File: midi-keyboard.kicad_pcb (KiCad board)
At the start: 2 copper layers, 87 parts, among them J1 ST7735R, SW1 SW_Push_45deg, SW10 SW_Push_45deg, SW11 SW_Push_45deg, SW12 SW_Push_45deg, SW13 SW_Push_45deg, SW14 SW_Push_45deg, SW15 SW_Push_45deg, SW16 SW_Push_45deg, SW17 SW_Push_45deg, SW18 SW_Push_45deg, SW19 SW_Push_45deg, SW2 SW_Push_45deg, SW20 SW_Push_45deg, SW21 SW_Push_45deg, SW22 SW_Push_45deg, SW23 SW_Push_45deg, SW24 SW_Push_45deg, SW25 SW_Push_45deg, SW26 SW_Push_45deg, SW27 SW_Push_45deg, SW28 SW_Push_45deg, SW29 SW_Push_45deg, SW3 SW_Push_45deg, SW30 SW_Push_45deg, SW31 SW_Push_45deg, SW32 SW_Push_45deg, SW33 SW_Push_45deg, SW34 SW_Push_45deg, SW35 SW_Push_45deg, SW36 SW_Push_45deg, SW37 SW_Push_45deg, SW38 SW_Push_45deg, SW39 SW_Push_45deg, SW4 SW_Push_45deg, SW40 SW_Push_45deg, SW42 RotaryEncoder_Switch_MP, SW43 RotaryEncoder_Switch_MP, SW44 SW_Push_45deg, SW5 SW_Push_45deg, SW6 SW_Push_45deg, SW7 SW_Push_45deg, SW8 SW_Push_45deg, SW9 SW_Push_45deg

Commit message: finished pcb tracing
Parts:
- removed D14, D21, D27, D28, D34, D35, D41, D42, D7: 1N4148, Diode_THT:D_DO-35_SOD27_P7.62mm_Horizontal
- removed SW34, SW35, SW36, SW37, SW38, SW39, SW40: SW_Push_45deg, Button_Switch_Keyboard:SW_Cherry_MX_1.00u_PCB
- removed SW42, SW43: RotaryEncoder_Switch_MP, Rotary_Encoder:RotaryEncoder_Alps_EC11E-Switch_Vertical_H20mm_MountingHoles
- J1: value ST7735R -> Conn_01x04; footprint Connector_PinHeader_2.54mm:PinHeader_1x08_P2.54mm_Vertical -> Connector_PinSocket_2.54mm:PinSocket_1x04_P2.54mm_Vertical
- SW44: footprint Button_Switch_Keyboard:SW_Cherry_MX_1.00u_PCB -> Button_Switch_THT:SW_PUSH_6mm
- moved SW27 321.6 mm to (82.3, 198.9)
- moved SW23 272.8 mm to (87.0, 170.3)
- moved SW24 267.1 mm to (120.4, 198.9)
- moved SW26 249.9 mm to (158.5, 198.9)
- moved SW25 249.6 mm to (139.4, 198.9)
- moved SW22 242.9 mm to (115.6, 170.3)
- moved A1 234.7 mm to (52.8, 158.2), turned to 90 degrees
- moved D22 230.6 mm to (114.4, 140.8)
- moved D23 224.5 mm to (124.2, 135.8)
- moved D24 210.4 mm to (153.8, 138.2)
- moved J1 208.9 mm to (106.5, 149.1)
- moved D26 200.5 mm to (183.0, 138.2)
- moved SW20 198.0 mm to (139.4, 146.5)
- moved D25 195.4 mm to (173.2, 138.2)
- moved SW30 180.9 mm to (196.6, 198.9)
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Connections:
- net 1S1 renamed ROW5
- A1 pad 10: COL1 -> unconnected-(A1-GPIO7-Pad10)
- A1 pad 11: COL2 -> unconnected-(A1-GPIO8-Pad11)
- A1 pad 12: COL3 -> unconnected-(A1-GPIO9-Pad12)
- A1 pad 14: COL4 -> unconnected-(A1-GPIO10-Pad14)
- A1 pad 15: COL5 -> unconnected-(A1-GPIO11-Pad15)
- A1 pad 16: COL6 -> unconnected-(A1-GPIO12-Pad16)
- A1 pad 17: A0 -> unconnected-(A1-GPIO13-Pad17)
- A1 pad 19: CS_SD -> SCL
- A1 pad 20: CS_LCD -> SDA
- A1 pad 21: MISO -> COL0
- A1 pad 22: 1A -> COL1
- A1 pad 24: SCK -> COL2
- A1 pad 25: MOSI -> COL3
- A1 pad 26: 1B -> COL4
- A1 pad 27: 2A -> COL5
- A1 pad 29: 2B -> unconnected-(A1-GPIO22-Pad29)
- A1 pad 31: BLCK -> unconnected-(A1-GPIO26_ADC0-Pad31)
- A1 pad 32: LRCLK -> unconnected-(A1-GPIO27_ADC1-Pad32)
- A1 pad 34: DIN -> unconnected-(A1-GPIO28_ADC2-Pad34)
- A1 pad 5: ROW3 -> ROW4
- A1 pad 7: 2S1 -> ROW3
- A1 pad 9: COL0 -> unconnected-(A1-GPIO6-Pad9)
- J1 pad 1: +3V3 -> GND
- J1 pad 2: SCK -> +3V3
- J1 pad 3: MOSI -> SCL
- J1 pad 4: A0 -> SDA
- SW10 pad 2: Net-(D10-A) -> Net-(D11-A)
- SW11 pad 2: Net-(D11-A) -> Net-(D12-A)
- SW12 pad 2: Net-(D12-A) -> Net-(D13-A)
- SW13 pad 1: ROW1 -> ROW2
- SW13 pad 2: Net-(D13-A) -> Net-(D15-A)
- SW14 pad 1: ROW1 -> ROW2
- SW14 pad 2: Net-(D28-A) -> Net-(D16-A)
- SW15 pad 2: Net-(D15-A) -> Net-(D17-A)
- SW16 pad 2: Net-(D16-A) -> Net-(D18-A)
- SW17 pad 2: Net-(D17-A) -> Net-(D19-A)
- SW18 pad 2: Net-(D18-A) -> Net-(D20-A)
- SW19 pad 1: ROW2 -> ROW3
- SW19 pad 2: Net-(D19-A) -> Net-(D22-A)
- SW20 pad 1: ROW2 -> ROW3
- SW20 pad 2: Net-(D20-A) -> Net-(D23-A)
- SW21 pad 1: ROW2 -> ROW3
- SW21 pad 2: Net-(D35-A) -> Net-(D24-A)
- SW22 pad 2: Net-(D22-A) -> Net-(D25-A)
- SW23 pad 2: Net-(D23-A) -> Net-(D26-A)
- SW24 pad 1: ROW3 -> ROW4
- SW24 pad 2: Net-(D24-A) -> Net-(D29-A)
- SW25 pad 1: ROW3 -> ROW4
- SW25 pad 2: Net-(D25-A) -> Net-(D30-A)
- SW26 pad 1: ROW3 -> ROW4
- SW26 pad 2: Net-(D26-A) -> Net-(D31-A)
- SW27 pad 1: ROW3 -> ROW4
- SW27 pad 2: Net-(D27-A) -> Net-(D32-A)
- SW28 pad 1: ROW3 -> ROW4
- SW28 pad 2: Net-(D42-A) -> Net-(D33-A)
- SW29 pad 2: Net-(D29-A) -> Net-(D36-A)
- SW30 pad 2: Net-(D30-A) -> Net-(D37-A)
- SW31 pad 2: Net-(D31-A) -> Net-(D38-A)
- SW32 pad 2: Net-(D32-A) -> Net-(D39-A)
- SW33 pad 2: Net-(D33-A) -> Net-(D40-A)
- SW7 pad 1: ROW0 -> ROW1
- SW7 pad 2: Net-(D21-A) -> Net-(D8-A)
- SW8 pad 2: Net-(D8-A) -> Net-(D9-A)
- SW9 pad 2: Net-(D9-A) -> Net-(D10-A)
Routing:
- net ROW2: track 0.00 -> 311.7 mm
- net ROW5: track 0.00 -> 239.8 mm
- net ROW1: track 0.00 -> 211.2 mm
- net Net-(D6-A): track 0.00 -> 204.8 mm, vias 0 -> 2
- net Net-(D4-A): track 0.00 -> 201.7 mm, vias 0 -> 2
- net Net-(D5-A): track 0.00 -> 199.6 mm, vias 0 -> 2
- net Net-(D3-A): track 0.00 -> 175.2 mm, vias 0 -> 2
- net Net-(D15-A): track 0.00 -> 173.8 mm, vias 0 -> 1
- net Net-(D32-A): track 0.00 -> 166.5 mm, vias 0 -> 2
- net Net-(D33-A): track 0.00 -> 166.4 mm, vias 0 -> 4
- net ROW4: track 0.00 -> 163.0 mm
- net Net-(D26-A): track 0.00 -> 161.0 mm, vias 0 -> 2
- net Net-(A1-RUN): track 0.00 -> 144.2 mm
- net Net-(D36-A): track 0.00 -> 133.3 mm, vias 0 -> 1
- net Net-(D2-A): track 0.00 -> 133.3 mm, vias 0 -> 2
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- added copper zone on B.Cu, net GND
- added copper zone on F.Cu, net GND
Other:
- board outline added: 171.8 x 108 mm

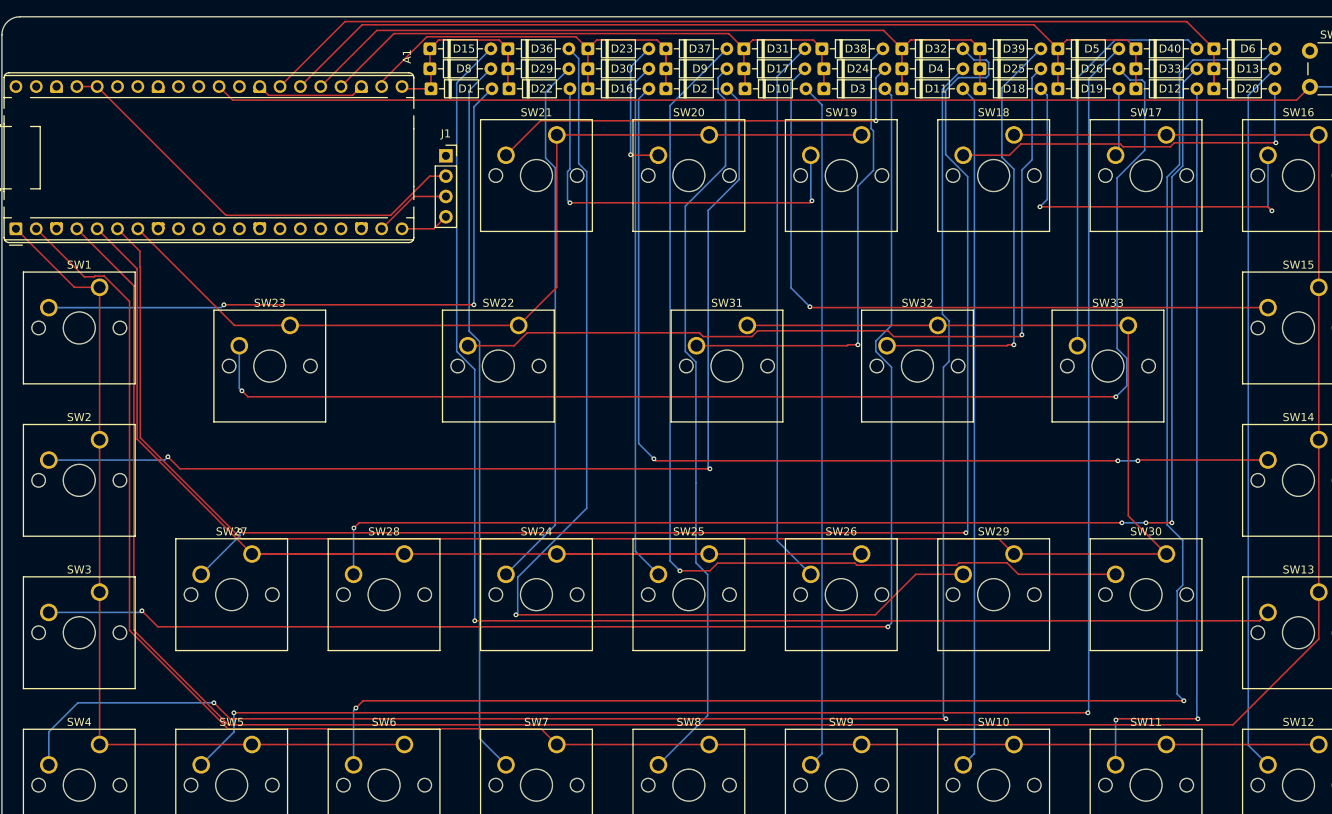
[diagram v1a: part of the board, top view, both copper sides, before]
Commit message: swap keys
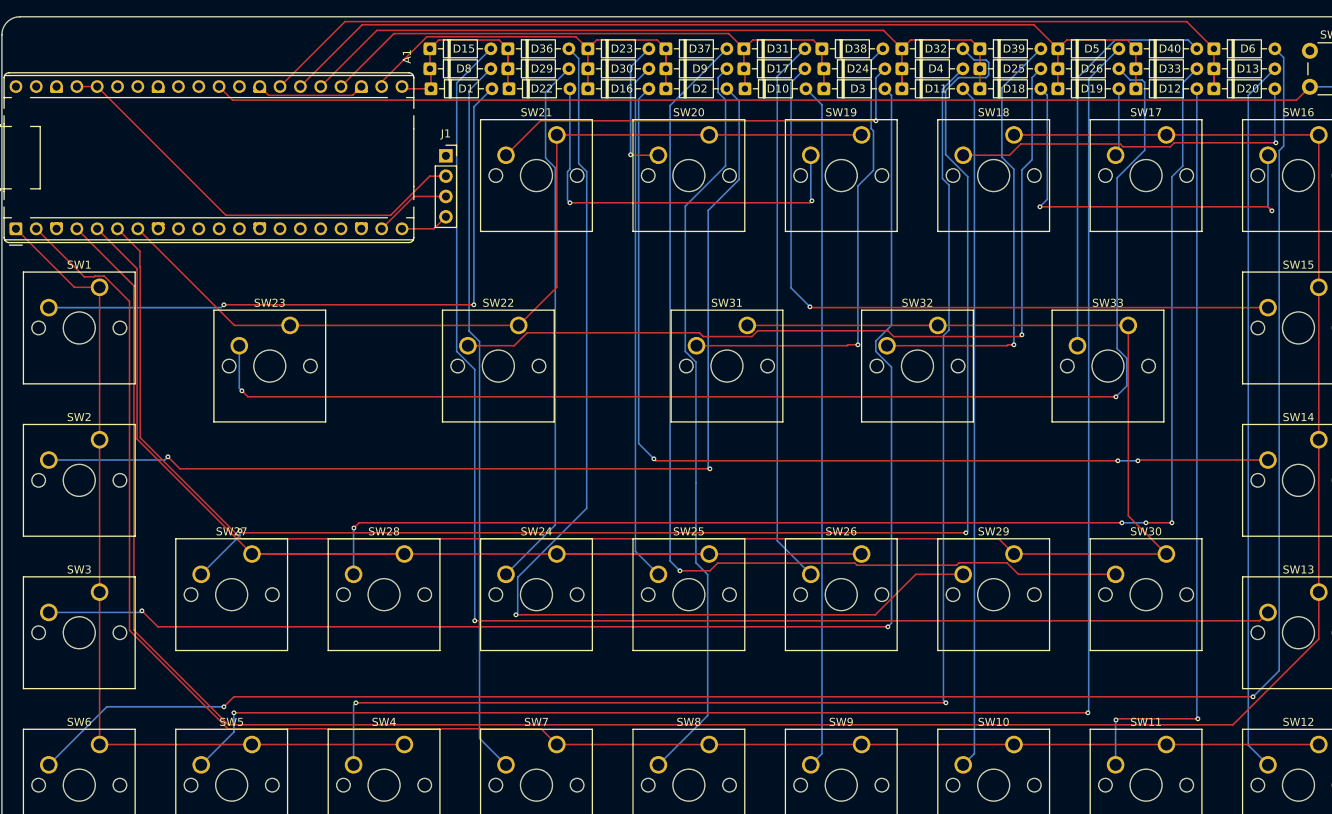
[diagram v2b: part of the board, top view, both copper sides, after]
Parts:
- moved SW4 38.1 mm to (101.3, 222.7)
- moved SW6 38.1 mm to (63.2, 222.7)
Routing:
- net Net-(D4-A): track 201.7 -> 162.7 mm
- net Net-(D6-A): track 204.8 -> 237.1 mm
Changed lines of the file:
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@@
 	(footprint "Button_Switch_Keyboard:SW_Cherry_MX_1.00u_PCB"
 		(layer "F.Cu")
-		(at 63.21 222.714)
+		(at 101.31 222.714)
 		(descr "Cherry MX keyswitch, 1.00u, PCB mount, http://cherryamericas.com/wp-content/uploads/2014/12/mx_cat.pdf")
 		(tags "Cherry MX keyswitch 1.00u PCB")
@@
 	(footprint "Button_Switch_Keyboard:SW_Cherry_MX_1.00u_PCB"
 		(layer "F.Cu")
-		(at 101.31 222.714)
+		(at 63.21 222.714)
 		(descr "Cherry MX keyswitch, 1.00u, PCB mount, http://cherryamericas.com/wp-content/uploads/2014/12/mx_cat.pdf")
 		(tags "Cherry MX keyswitch 1.00u PCB")
@@
 	)
 	(segment
+		(start 63.21 165.564)
+		(end 60.064 165.564)
+		(width 0.2)
+		(layer "F.Cu")
+		(net "ROW0")
+	)
+	(segment
 		(start 82.26 222.714)
 		(end 101.31 222.714)
@@
 	)
 	(segment
-		(start 63.21 165.564)
-		(end 60.064 165.564)
-		(width 0.2)
-		(layer "F.Cu")
-		(net "ROW0")
-	)
-	(segment
 		(start 60.064 165.564)
 		(end 52.75 158.25)
@@
 	)
 	(segment
-		(start 79.5 219.5)
-		(end 77.5 217.5)
-		(width 0.2)
-		(layer "F.Cu")
-		(net "Net-(D4-A)")
-	)
-	(segment
-		(start 169 219.5)
-		(end 79.5 219.5)
+		(start 95.25 217.5)
+		(end 169 217.5)
 		(width 0.2)
 		(layer "F.Cu")
@@
 	)
 	(via
-		(at 77.5 217.5)
+		(at 95.25 217.5)
 		(size 0.6)
 		(drill 0.3)
@@
 	)
 	(via
-		(at 169 219.5)
+		(at 169 217.5)
 		(size 0.6)
 		(drill 0.3)
@@
 	)
 	(segment
-		(start 168.564899 140.805101)
-		(end 168.564899 168.9265)
+		(start 168.69 217.19)
+		(end 168.69 171.601399)
 		(width 0.2)
 		(layer "B.Cu")
@@
 	)
 	(segment
-		(start 77.5 217.5)
-		(end 60.5 217.5)
-		(width 0.2)
-		(layer "B.Cu")
-		(net "Net-(D4-A)")
-	)
-	(segment
-		(start 168.69 175.544444)
-		(end 168.69 219.19)
+		(start 168.564899 151.965955)
+		(end 168.564899 140.805101)
 		(width 0.2)
 		(layer "B.Cu")
@@
 	)
 	(segment
-		(start 171.12 138.25)
-		(end 168.564899 140.805101)
+		(start 169.385 170.906399)
+		(end 169.385 152.786056)
 		(width 0.2)
 		(layer "B.Cu")
@@
 	)
 	(segment
-		(start 168.564899 168.9265)
-		(end 169.385 169.746601)
+		(start 94.96 217.79)
+		(end 95.25 217.5)
 		(width 0.2)
 		(layer "B.Cu")
@@
 	)
 	(segment
-		(start 169.385 174.849444)
-		(end 168.69 175.544444)
+		(start 168.564899 140.805101)
+		(end 171.12 138.25)
 		(width 0.2)
 		(layer "B.Cu")
@@
 	)
 	(segment
-		(start 60.5 217.5)
-		(end 56.86 221.14)
+		(start 169 217.5)
+		(end 168.69 217.19)
 		(width 0.2)
 		(layer "B.Cu")
@@
 	)
 	(segment
-		(start 168.69 219.19)
-		(end 169 219.5)
+		(start 169.385 152.786056)
+		(end 168.564899 151.965955)
 		(width 0.2)
 		(layer "B.Cu")
@@
 	)
 	(segment
-		(start 169.385 169.746601)
-		(end 169.385 174.849444)
+		(start 168.69 171.601399)
+		(end 169.385 170.906399)
 		(width 0.2)
 		(layer "B.Cu")
@@
 	)
 	(segment
-		(start 56.86 221.14)
-		(end 56.86 225.254)
+		(start 94.96 225.254)
+		(end 94.96 217.79)
 		(width 0.2)
 		(layer "B.Cu")
@@
 	)
 	(segment
-		(start 198.75 217.25)
-		(end 96.15 217.25)
+		(start 78.75 218)
+		(end 80 216.75)
 		(width 0.2)
 		(layer "F.Cu")
@@
 	)
 	(segment
-		(start 96.15 217.25)
-		(end 95.25 218.15)
+		(start 80 216.75)
+		(end 207.39 216.75)
 		(width 0.2)
 		(layer "F.Cu")
@@
 	)
 	(via
-		(at 198.75 217.25)
+		(at 78.75 218)
 		(size 0.6)
 		(drill 0.3)
@@
 	)
 	(via
-		(at 95.25 218.15)
+		(at 207.39 216.75)
 		(size 0.6)
 		(drill 0.3)
@@
 	)
 	(segment
-		(start 199.914365 137.15)
-		(end 198.202944 138.861421)
-		(width 0.2)
-		(layer "B.Cu")
-		(net "Net-(D6-A)")
-	)
-	(segment
-		(start 198.602944 202.7815)
-		(end 197.9 203.484444)
-		(width 0.2)
-		(layer "B.Cu")
-		(net "Net-(D6-A)")
-	)
-	(segment
-		(start 197.9 203.484444)
-		(end 197.9 216.4)
-		(width 0.2)
-		(layer "B.Cu")
-		(net "Net-(D6-A)")
-	)
-	(segment
-		(start 210.12 135.75)
-		(end 208.72 137.15)
-		(width 0.2)
-		(layer "B.Cu")
-		(net "Net-(D6-A)")
-	)
-	(segment
-		(start 197.9 216.4)
-		(end 198.75 217.25)
-		(width 0.2)
-		(layer "B.Cu")
-		(net "Net-(D6-A)")
-	)
-	(segment
-		(start 95.25 218.15)
-		(end 94.96 218.44)
-		(width 0.2)
-		(layer "B.Cu")
-		(net "Net-(D6-A)")
-	)
-	(segment
-		(start 208.72 137.15)
-		(end 199.914365 137.15)
+		(start 211.22 136.85)
+		(end 210.12 135.75)
 		(width 0.2)
 		(layer "B.Cu")
@@
 	)
 	(segment
-		(start 198.602944 197.201473)
-		(end 198.602944 202.7815)
+		(start 56.86 225.254)
+		(end 64.114 218)
 		(width 0.2)
 		(layer "B.Cu")
@@
 	)
 	(segment
-		(start 198.202944 150.228314)
-		(end 196.65 151.781258)
+		(start 207.39 216.75)
+		(end 210.66 213.48)
 		(width 0.2)
 		(layer "B.Cu")
@@
 	)
 	(segment
-		(start 94.96 218.44)
-		(end 94.96 225.254)
+		(start 210.66 213.48)
+		(end 210.66 148.474101)
 		(width 0.2)
 		(layer "B.Cu")
@@
 	)
 	(segment
-		(start 196.65 151.781258)
-		(end 196.65 195.248529)
+		(start 64.114 218)
+		(end 78.75 218)
 		(width 0.2)
 		(layer "B.Cu")
@@
 	)
 	(segment
-		(start 198.202944 138.861421)
-		(end 198.202944 150.228314)
+		(start 210.66 148.474101)
+		(end 211.22 147.914101)
 		(width 0.2)
 		(layer "B.Cu")
@@
 	)
 	(segment
-		(start 196.65 195.248529)
-		(end 198.602944 197.201473)
+		(start 211.22 147.914101)
+		(end 211.22 136.85)
 		(width 0.2)
 		(layer "B.Cu")
